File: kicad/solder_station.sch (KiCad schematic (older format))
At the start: 38 parts, among them IC1 ATMEGA328-P, P1 CONN_01X05, P2 CONN_01X02, P3 Standby, P4 UART, Q1 2N7000, Q2 IRF4905, U1 LM2596_module, U2 AD8551, U3 EC11, Y1 16MHz

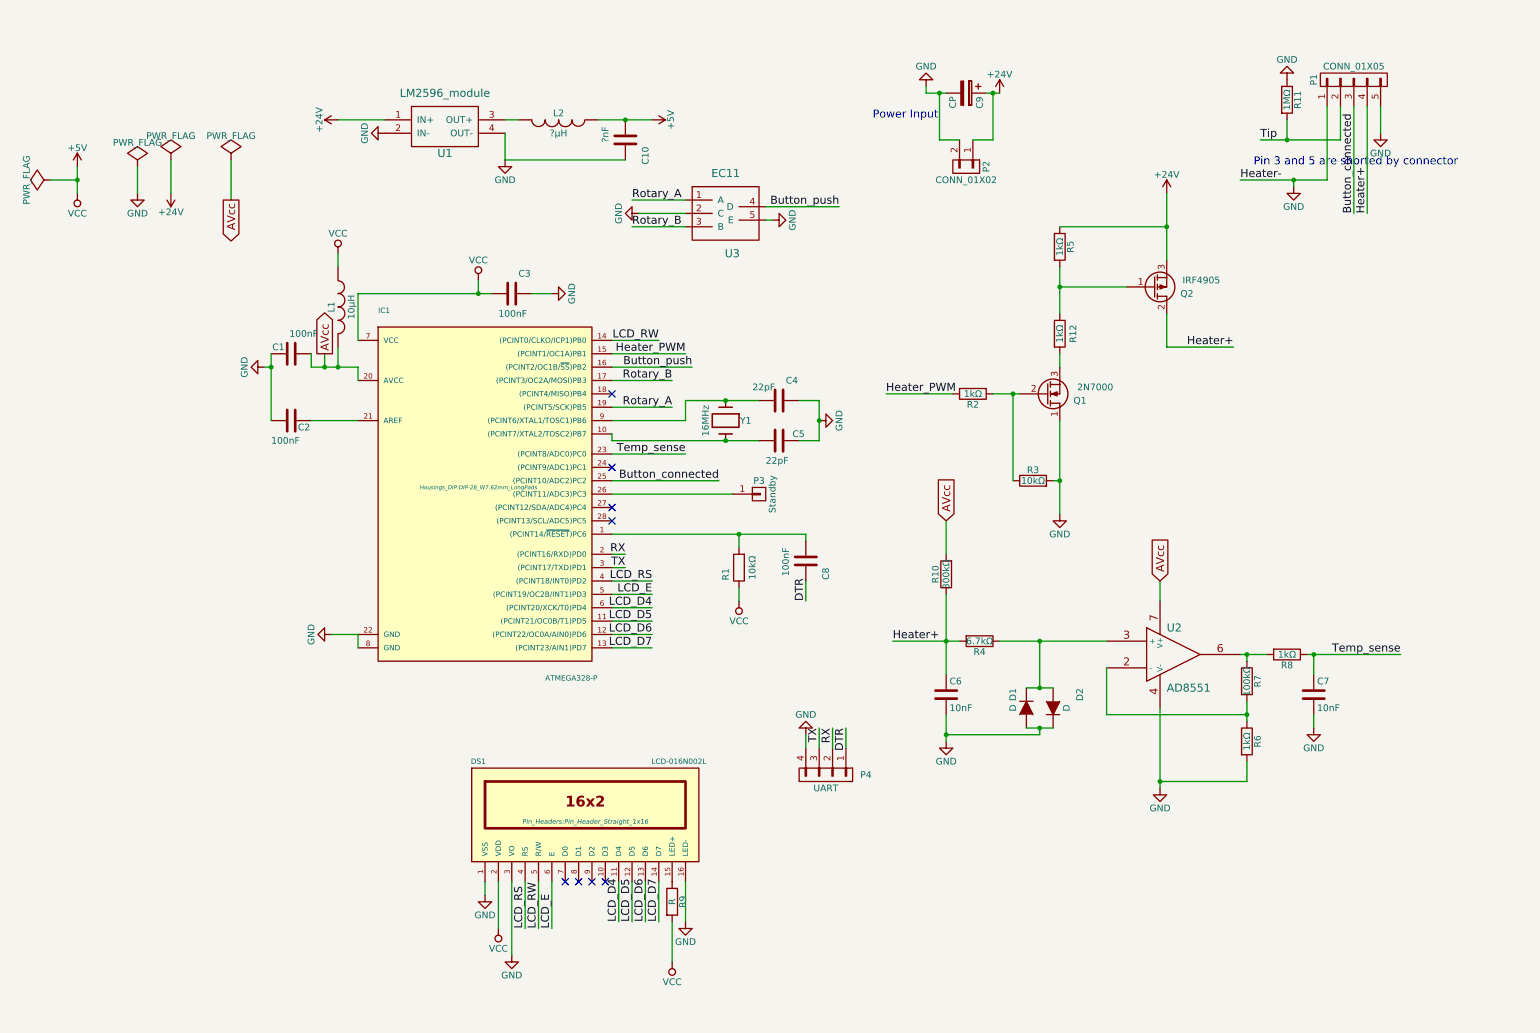
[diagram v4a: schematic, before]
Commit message: [Kicad] Use more capacitors and smd parts
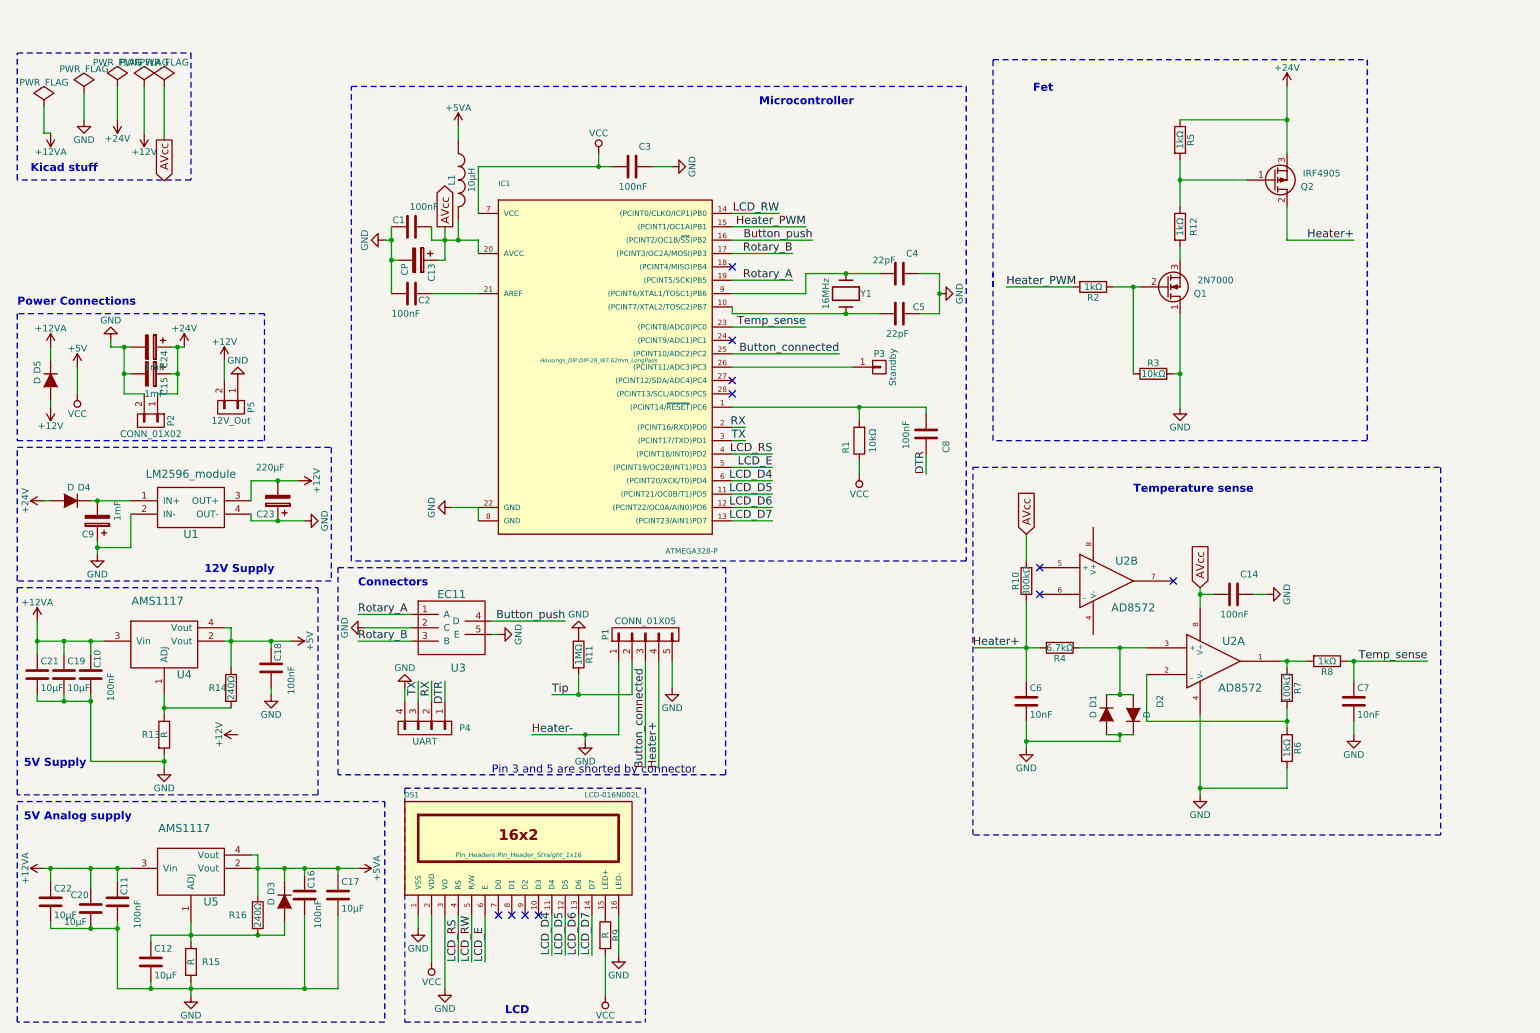
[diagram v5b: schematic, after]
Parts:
- removed L2: ?µH, Choke_Axial_ThroughHole:Choke_Horizontal_RM10mm, symbol INDUCTOR
- removed U2: AD8551, Housings_SOIC:SOIC-8_3.9x4.9mm_Pitch1.27mm, symbol TL071
- added C11, C14, C16, C18: 100nF, Capacitors_SMD:C_0603, symbol C
- added C12, C17, C19, C20, C21, C22: 10µF, Capacitors_SMD:C_0603, symbol C
- added C13: CP, Capacitors_ThroughHole:C_Radial_D6.3_L11.2_P2.5, symbol CP
- added C15, C24: 1mF, Capacitors_ThroughHole:C_Radial_D6.3_L11.2_P2.5, symbol CP
- added C23: 220µF, Capacitors_ThroughHole:C_Radial_D6.3_L11.2_P2.5, symbol CP
- added D3, D4, D5: D, Diodes_ThroughHole:Diode_DO-35_SOD27_Horizontal_RM10, symbol D
- added P5: 12V_Out, Pin_Headers:Pin_Header_Angled_1x02, symbol CONN_01X02
- added R13, R15: R, Resistors_SMD:R_0805, symbol R
- added R14, R16: 240Ω, Resistors_SMD:R_0805, symbol R
- added U2: AD8572, Housings_SOIC:SOIC-8_3.9x4.9mm_Pitch1.27mm, symbol LM293
- added U4, U5: AMS1117, TO_SOT_Packages_SMD:SOT-223, symbol AMS1117
- C1, C2, C3, C8: footprint Capacitors_SMD:C_0603_HandSoldering -> Capacitors_SMD:C_0603
- C10: value ?nF -> 100nF; footprint Capacitors_SMD:C_0603_HandSoldering -> Capacitors_SMD:C_0603
- C9: value CP -> 1mF
- R11, R3, R6, R7: footprint Resistors_ThroughHole:Resistor_Horizontal_RM10mm -> Resistors_SMD:R_0805
- R4: footprint Resistors_ThroughHole:Resistor_Horizontal_RM10mm -> Resistors_SMD:R_0805_HandSoldering
- R8: footprint Resistors_ThroughHole:Resistor_Horizontal_RM10mm -> Resistors_ThroughHole:Resistor_Horizontal_RM7mm
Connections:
- net +24V: now also C15.1, C24.1, D4.2 (A); no longer C9.1, U1.1 (IN+)
- net +5V: now also C18.1, R14.1, U4.2 (Vout), U4.4 (Vout); no longer C10.2, L1.1
- net AVcc: now also C13.1, C14.2, U2.8 (V+)
- net GND: now also C10.2, C9.1, C11.2, C12.2, C13.2, C14.1, C15.2, C16.2, C17.2, C18.2, C19.2, C20.2, C21.2, C22.2, C23.1, C24.2, P5.1 (P1), R13.2, R15.2, U2.4 (V-); no longer C10.1, C9.2
- net at R6.1, R7.2: now also U2.2 (_)
- net at R7.1, R8.2: now also U2.1
- net at D1.1 (K), D2.2 (A), R4.1: now also U2.3 (+)
- net +12V: now reaches U1.3 (OUT+)
- net +12V: now also C23.2, D5.2 (A), P5.2 (P2)
- new net: C9.2, D4.1 (K), U1.1 (IN+)
- new net: C12.1, D3.2 (A), R15.1, R16.2, U5.1 (ADJ)
- new net: R13.1, R14.2, U4.1 (ADJ)
- new net +12VA: C10.1, C11.1, C19.1, C20.1, C21.1, C22.1, D5.1 (K), U4.3 (Vin), U5.3 (Vin)
- new net +5VA: C16.1, C17.1, D3.1 (K), L1.1, R16.1, U5.2 (Vout), U5.4 (Vout)
- no-connect marks 8 -> 11
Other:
- note added: "12V Supply"
- note added: "5V Analog supply"
- note added: "5V Supply"
- note added: "Connectors"
- note added: "Fet"
- note added: "Kicad stuff"
- note added: "LCD"
- note added: "Microcontroller"
- note added: "Power Connections"
- note added: "Temperature sense"
- note removed: "Power Input"
- moved on the sheet: C1, C2, C3, C4, C5, C6, C7, C8, C9, D1, D2, DS1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

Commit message: [Kicad] Update (forgot to save).
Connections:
- net +12V: now also C23.1; no longer C23.2
- net GND: now also C23.2, C9.2; no longer C23.1, C9.1
- net at D4.1 (K), U1.1 (IN+): now also C9.1; no longer C9.2
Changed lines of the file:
@@
 F 3 "" H 1100 4000 60  0000 C CNN
 	1    1100 4000
-	-1   0    0    1
+	1    0    0    -1
 $EndComp
 $Comp
@@
 $EndComp
 $Comp
-L +12V #PWR038
-U 1 1 56CECF06
-P 2150 5600
-F 0 "#PWR038" H 2150 5450 50  0001 C CNN
-F 1 "+12V" H 2150 5740 50  0000 C CNN
-F 2 "" H 2150 5600 60  0000 C CNN
-F 3 "" H 2150 5600 60  0000 C CNN
-	1    2150 5600
-	0    -1   -1   0
-$EndComp
-$Comp
 L R R16
 U 1 1 56CECF0D
@@
 $EndComp
 $Comp
-L GND #PWR039
+L GND #PWR038
 U 1 1 56CECF15
 P 1800 7550
-F 0 "#PWR039" H 1800 7300 50  0001 C CNN
+F 0 "#PWR038" H 1800 7300 50  0001 C CNN
 F 1 "GND" H 1800 7400 50  0000 C CNN
 F 2 "" H 1800 7550 60  0000 C CNN
@@
 $EndComp
 $Comp
-L +5VA #PWR040
+L +5VA #PWR039
 U 1 1 56CED85F
 P 3050 6600
-F 0 "#PWR040" H 3050 6450 50  0001 C CNN
+F 0 "#PWR039" H 3050 6450 50  0001 C CNN
 F 1 "+5VA" H 3050 6740 50  0000 C CNN
 F 2 "" H 3050 6600 60  0000 C CNN
@@
 AVcc
 $Comp
-L PWR_FLAG #FLG041
+L PWR_FLAG #FLG040
 U 1 1 56CEF538
 P 1600 750
-F 0 "#FLG041" H 1600 845 50  0001 C CNN
+F 0 "#FLG040" H 1600 845 50  0001 C CNN
 F 1 "PWR_FLAG" H 1600 930 50  0000 C CNN
 F 2 "" H 1600 750 60  0000 C CNN
@@
 $EndComp
 $Comp
-L +12V #PWR042
+L +12V #PWR041
 U 1 1 56CEF85B
 P 1450 1100
-F 0 "#PWR042" H 1450 950 50  0001 C CNN
+F 0 "#PWR041" H 1450 950 50  0001 C CNN
 F 1 "+12V" H 1450 1240 50  0000 C CNN
 F 2 "" H 1450 1100 60  0000 C CNN
@@
 $EndComp
 $Comp
-L PWR_FLAG #FLG043
+L PWR_FLAG #FLG042
 U 1 1 56CEFE12
 P 1450 750
-F 0 "#FLG043" H 1450 845 50  0001 C CNN
+F 0 "#FLG042" H 1450 845 50  0001 C CNN
 F 1 "PWR_FLAG" H 1450 930 50  0000 C CNN
 F 2 "" H 1450 750 60  0000 C CNN
@@
 $EndComp
 $Comp
-L +12V #PWR044
+L +12V #PWR043
 U 1 1 56CE6F4D
 P 2050 2800
-F 0 "#PWR044" H 2050 2650 50  0001 C CNN
+F 0 "#PWR043" H 2050 2650 50  0001 C CNN
 F 1 "+12V" H 2050 2940 50  0000 C CNN
 F 2 "" H 2050 2800 60  0000 C CNN
@@
 $EndComp
 $Comp
-L GND #PWR045
+L GND #PWR044
 U 1 1 56CE70FF
 P 2150 2950
-F 0 "#PWR045" H 2150 2700 50  0001 C CNN
+F 0 "#PWR044" H 2150 2700 50  0001 C CNN
 F 1 "GND" H 2150 2800 50  0000 C CNN
 F 2 "" H 2150 2950 60  0000 C CNN
@@
 $EndComp
 $Comp
-L GND #PWR046
+L GND #PWR045
 U 1 1 56D13D14
 P 9850 4550
-F 0 "#PWR046" H 9850 4300 50  0001 C CNN
+F 0 "#PWR045" H 9850 4300 50  0001 C CNN
 F 1 "GND" H 9850 4400 50  0000 C CNN
 F 2 "" H 9850 4550 60  0000 C CNN
@@
 U 1 1 56D4E355
 P 1500 2900
-F 0 "C15" H 1525 3000 50  0000 L CNN
-F 1 "1mF" V 1650 2850 50  0000 L CNN
+F 0 "C15" V 1600 2950 50  0000 L CNN
+F 1 "1mF" V 1600 2700 50  0000 L CNN
 F 2 "Capacitors_ThroughHole:C_Radial_D6.3_L11.2_P2.5" H 1538 2750 30  0001 C CNN
 F 3 "" H 1500 2900 60  0000 C CNN
@@
 $EndComp
 $Comp
-L GND #PWR047
+L GND #PWR046
 U 1 1 56D7044A
 P 2400 5300
-F 0 "#PWR047" H 2400 5050 50  0001 C CNN
+F 0 "#PWR046" H 2400 5050 50  0001 C CNN
 F 1 "GND" H 2400 5150 50  0000 C CNN
 F 2 "" H 2400 5300 60  0000 C CNN
@@
 F 3 "" H 2450 3850 60  0000 C CNN
 	1    2450 3850
-	-1   0    0    1
+	1    0    0    -1
 $EndComp
 $Comp
@@
 Connection ~ 1050 7050
 $Comp
-L +12VA #PWR048
+L +12VA #PWR047
 U 1 1 56D78BF6
 P 650 4750
-F 0 "#PWR048" H 650 4600 50  0001 C CNN
+F 0 "#PWR047" H 650 4600 50  0001 C CNN
 F 1 "+12VA" H 650 4890 50  0000 C CNN
 F 2 "" H 650 4750 60  0000 C CNN
@@
 $EndComp
 $Comp
-L +12VA #PWR049
+L +12VA #PWR048
 U 1 1 56D78DE8
 P 700 6600
-F 0 "#PWR049" H 700 6450 50  0001 C CNN
+F 0 "#PWR048" H 700 6450 50  0001 C CNN
 F 1 "+12VA" H 700 6740 50  0000 C CNN
 F 2 "" H 700 6600 60  0000 C CNN
@@
 Connection ~ 750  6600
 $Comp
-L +12VA #PWR050
+L +12VA #PWR049
 U 1 1 56D7A5CF
 P 750 2700
-F 0 "#PWR050" H 750 2550 50  0001 C CNN
+F 0 "#PWR049" H 750 2550 50  0001 C CNN
 F 1 "+12VA" H 750 2840 50  0000 C CNN
 F 2 "" H 750 2700 60  0000 C CNN
@@
 $EndComp
 $Comp
-L +12V #PWR051
+L +12V #PWR050
 U 1 1 56D7A68E
 P 750 3150
-F 0 "#PWR051" H 750 3000 50  0001 C CNN
+F 0 "#PWR050" H 750 3000 50  0001 C CNN
 F 1 "+12V" H 750 3290 50  0000 C CNN
 F 2 "" H 750 3150 60  0000 C CNN
@@
 	1350 4200 1100 4200
 $Comp
-L +12VA #PWR052
+L +12VA #PWR051
 U 1 1 56D7E71A
 P 750 1100
-F 0 "#PWR052" H 750 950 50  0001 C CNN
+F 0 "#PWR051" H 750 950 50  0001 C CNN
 F 1 "+12VA" H 750 1240 50  0000 C CNN
 F 2 "" H 750 1100 60  0000 C CNN
@@
 $EndComp
 $Comp
-L PWR_FLAG #FLG053
+L PWR_FLAG #FLG052
 U 1 1 56D7ED57
 P 700 900
-F 0 "#FLG053" H 700 995 50  0001 C CNN
+F 0 "#FLG052" H 700 995 50  0001 C CNN
 F 1 "PWR_FLAG" H 700 1080 50  0000 C CNN
 F 2 "" H 700 900 60  0000 C CNN
@@
 U 1 1 56D808BA
 P 1500 2700
-F 0 "C24" H 1525 2800 50  0000 L CNN
-F 1 "1mF" V 1650 2650 50  0000 L CNN
+F 0 "C24" V 1550 2750 50  0000 L CNN
+F 1 "1mF" V 1350 2650 50  0000 L CNN
 F 2 "Capacitors_ThroughHole:C_Radial_D6.3_L11.2_P2.5" H 1538 2550 30  0001 C CNN
 F 3 "" H 1500 2700 60  0000 C CNN

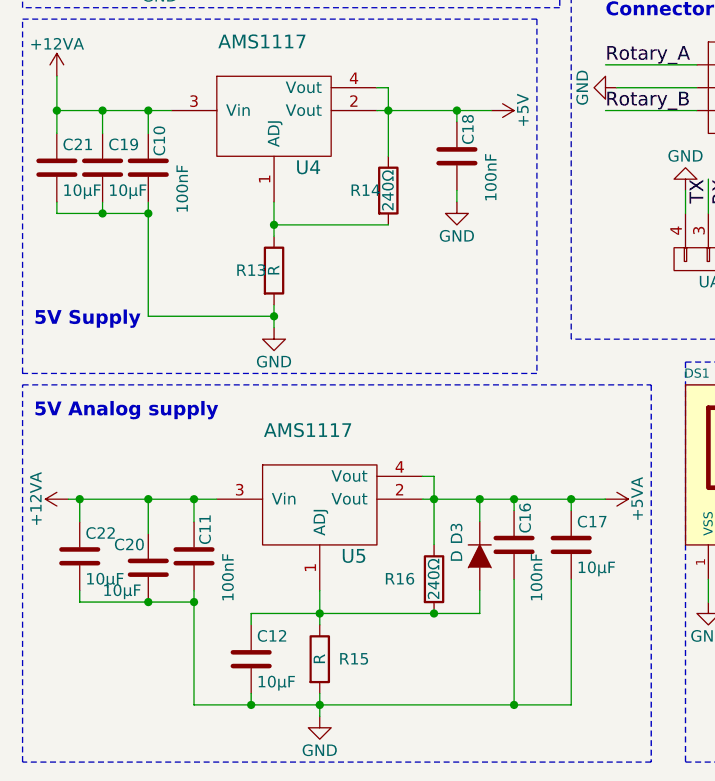
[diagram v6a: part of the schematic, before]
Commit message: [Kicad] Add resistor values for voltage regulators.
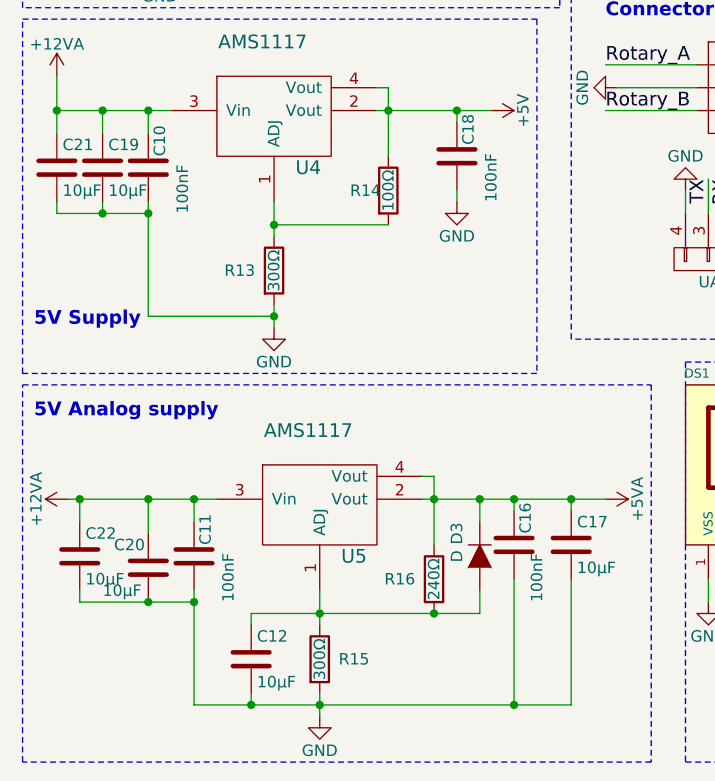
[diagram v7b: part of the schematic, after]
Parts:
- R13, R15: value R -> 300Ω
- R14: value 240Ω -> 100Ω
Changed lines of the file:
@@
 P 2100 5250
 F 0 "R14" H 2000 5250 50  0000 C CNN
-F 1 "240Ω" V 2100 5250 50  0000 C CNN
+F 1 "100Ω" V 2100 5250 50  0000 C CNN
 F 2 "Resistors_SMD:R_0805" V 2030 5250 30  0001 C CNN
 F 3 "" H 2100 5250 30  0000 C CNN
@@
 U 1 1 56CE998F
 P 1600 5600
-F 0 "R13" H 1500 5600 50  0000 C CNN
-F 1 "R" V 1600 5600 50  0000 C CNN
+F 0 "R13" H 1450 5600 50  0000 C CNN
+F 1 "300Ω" V 1600 5600 50  0000 C CNN
 F 2 "Resistors_SMD:R_0805" V 1530 5600 30  0001 C CNN
 F 3 "" H 1600 5600 30  0000 C CNN
@@
 P 1800 7300
 F 0 "R15" H 1950 7300 50  0000 C CNN
-F 1 "R" V 1800 7300 50  0000 C CNN
+F 1 "300Ω" V 1800 7300 50  0000 C CNN
 F 2 "Resistors_SMD:R_0805" V 1730 7300 30  0001 C CNN
 F 3 "" H 1800 7300 30  0000 C CNN

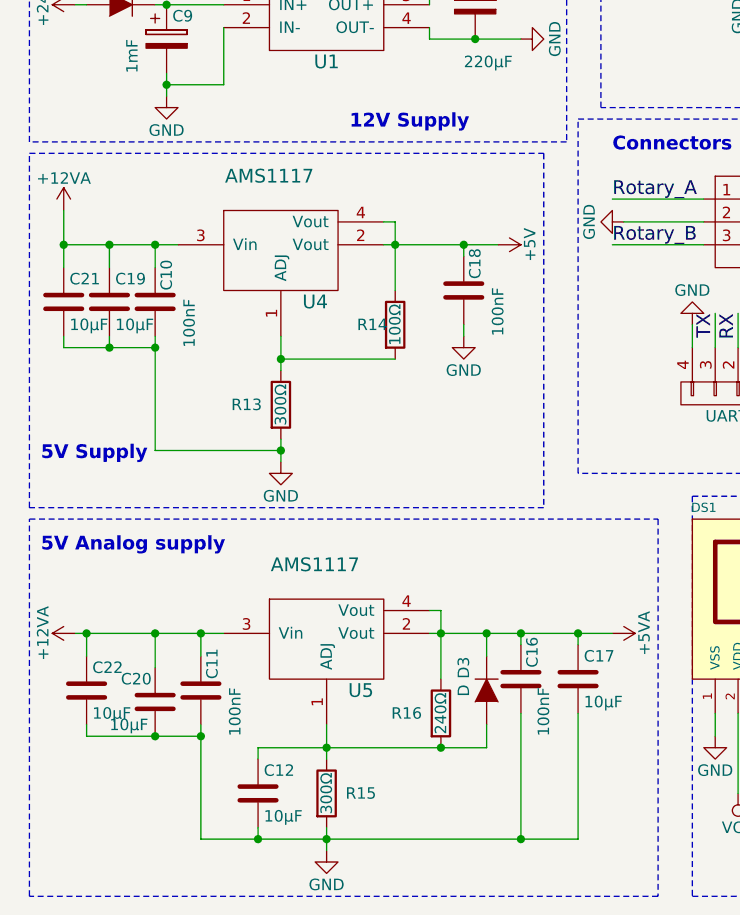
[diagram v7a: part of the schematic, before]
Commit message: [Kicad] Add a few more capacitors.
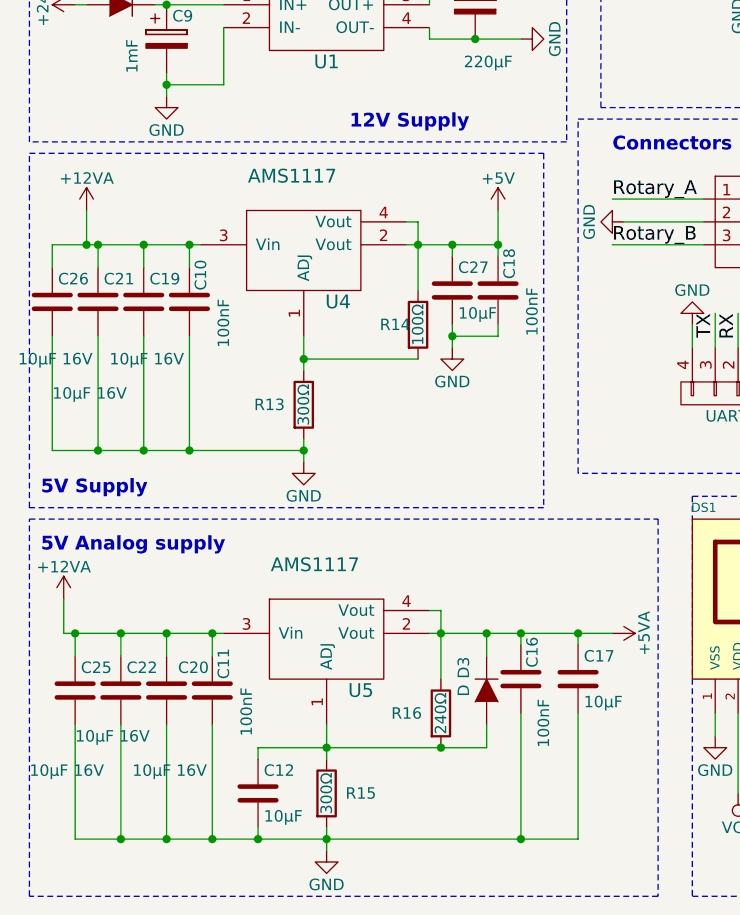
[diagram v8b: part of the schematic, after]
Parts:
- added C25, C26: 10µF 16V, Capacitors_SMD:C_0805, symbol C
- added C27: 10µF, Capacitors_SMD:C_0603, symbol C
- C19, C20, C21, C22: value 10µF -> 10µF 16V; footprint Capacitors_SMD:C_0603 -> Capacitors_SMD:C_0805
- C6, C7: footprint Capacitors_ThroughHole:C_Disc_D3_P2.5 -> Capacitors_SMD:C_0603
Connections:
- net +12VA: now also C25.1, C26.1
- net +5V: now also C27.1
- net GND: now also C25.2, C26.2, C27.2
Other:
- moved on the sheet: C10, C11, C18, C19, C20, C21, C22, R13, R14, U4
